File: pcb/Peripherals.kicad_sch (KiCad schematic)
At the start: 29 parts, among them Q4 SS8050, U10 LSM6DSMTR, U11 LIS2MDL, U15 ISO1044BD, U2 MKDV32GCL-STP, U9 MS5607-02BA

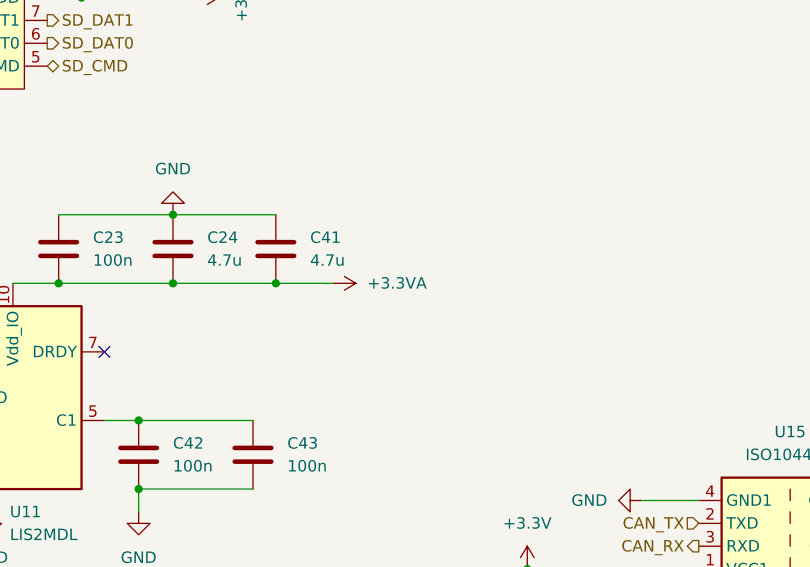
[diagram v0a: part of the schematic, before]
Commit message: added active gps antenna connector
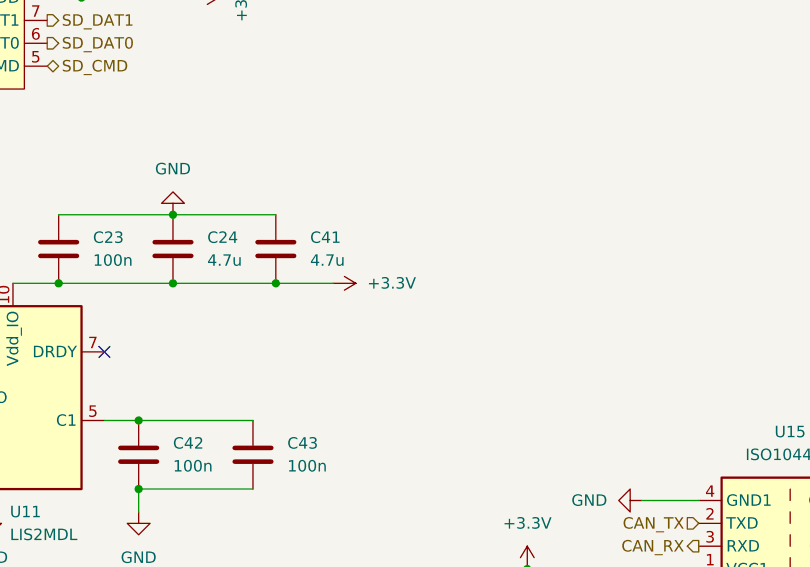
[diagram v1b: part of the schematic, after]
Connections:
- net +3.3V: now also C23.2, C24.2, C41.2, U11.10 (Vdd_IO)
- net +3.3VA: no longer C23.2, C24.2, C41.2, U11.10 (Vdd_IO)
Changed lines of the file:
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@@
 			)
 		)
-		(property "Value" "+3.3VA"
+		(property "Value" "+3.3V"
 			(at 181.61 107.9499 90)
 			(effects

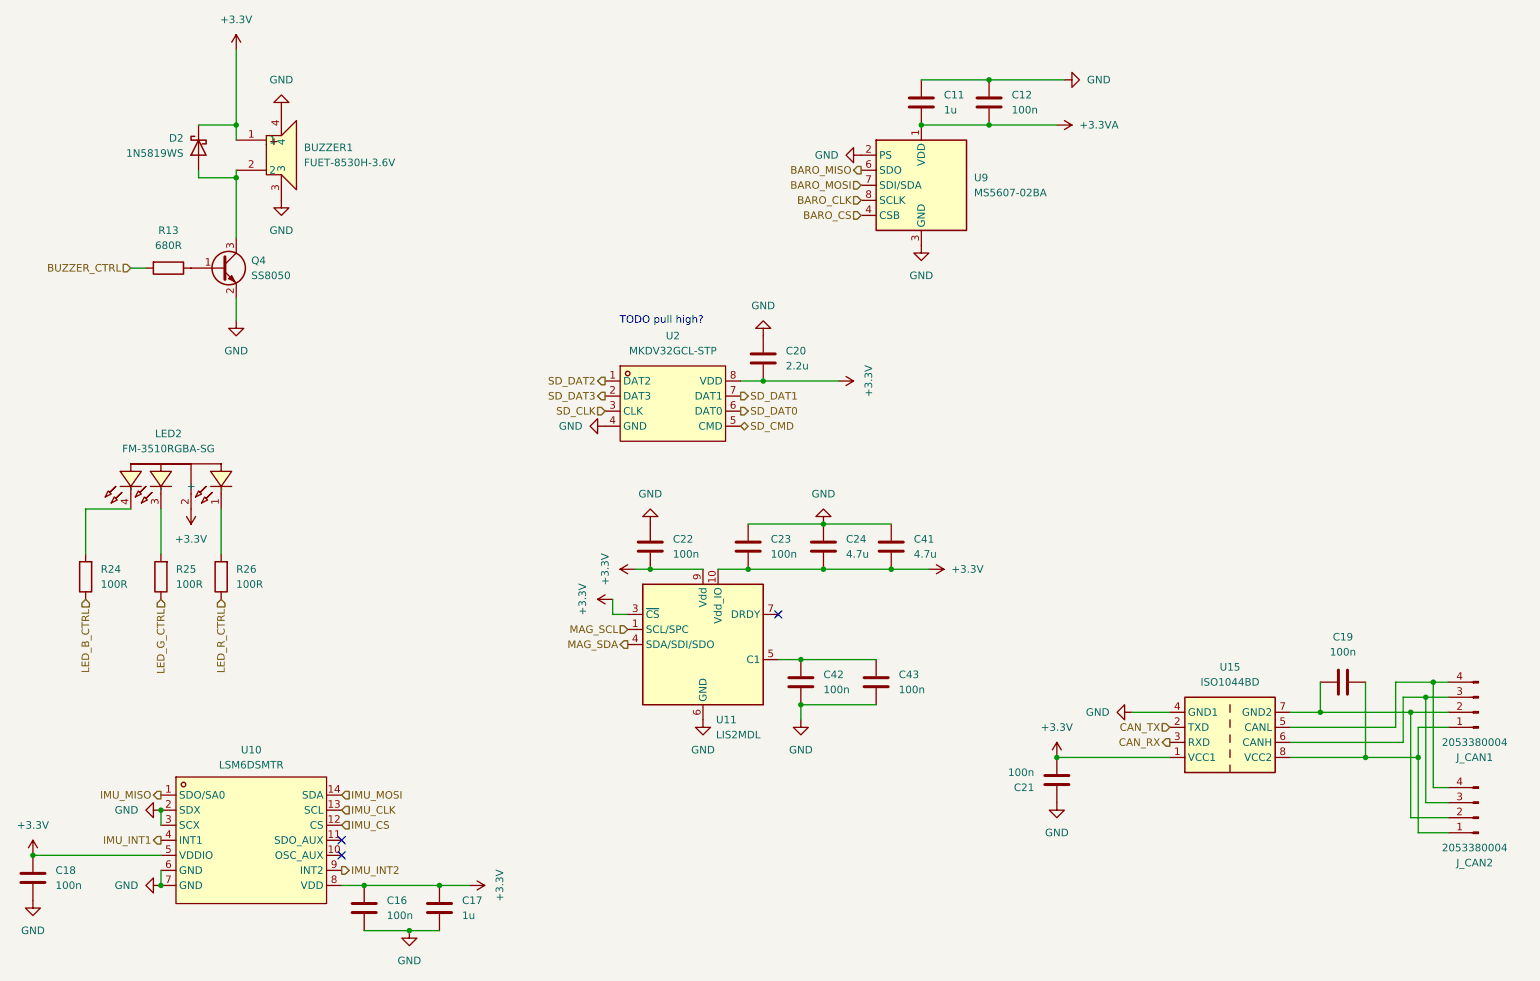
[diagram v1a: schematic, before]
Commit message: add pull up resistor for sd, change pad net
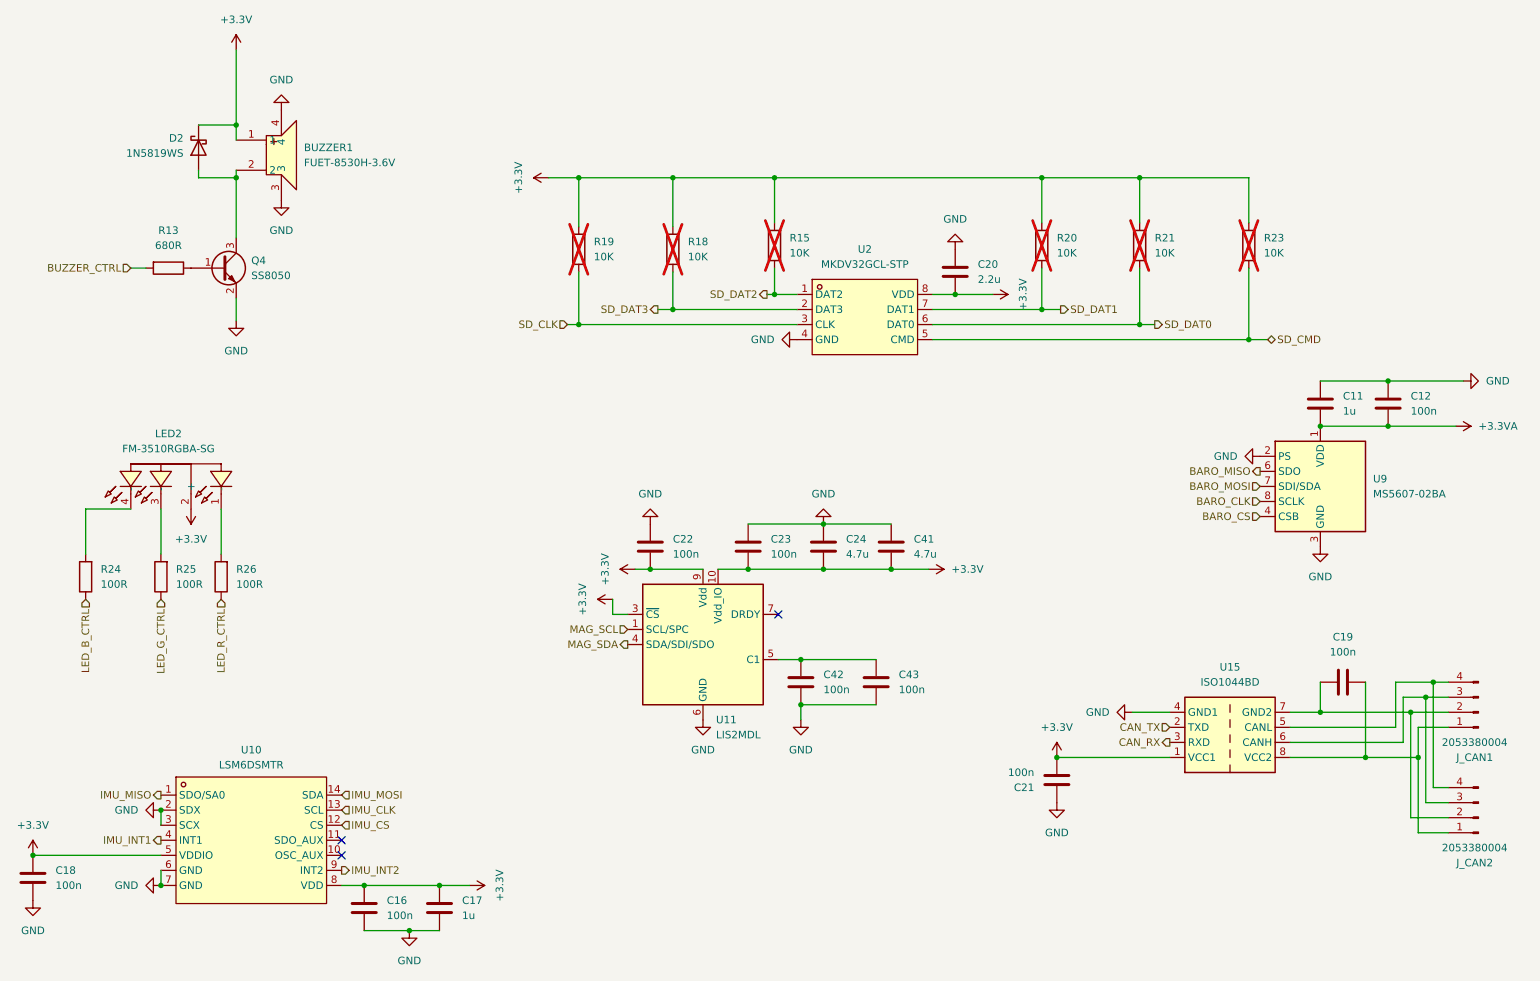
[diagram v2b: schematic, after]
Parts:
- added R15, R18, R19, R20, R21, R23: 10K, Resistor_SMD:R_0603_1608Metric_Pad0.98x0.95mm_HandSolder, symbol Device:R
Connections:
- net +3.3V: now also R15.2, R18.2, R19.2, R20.2, R21.2, R23.2
- net SD_CLK: now also R19.1
- net SD_CMD: now also R23.1
- net SD_DAT0: now also R21.1
- net SD_DAT1: now also R20.1
- net SD_DAT2: now also R15.1
- net SD_DAT3: now also R18.1
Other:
- note removed: "TODO pull high?"
- moved on the sheet: C11, C12, C20, U2, U9
